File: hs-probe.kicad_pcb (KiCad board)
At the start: 4 copper layers, 36.5 x 14 mm, 52 parts, among them J1 USB_C_Receptacle_USB2.0, J2 Castellated Vias, J3 Castellated Vias, J4 Castellated Vias, U1 STM32F723IEKx, U2 DSC6003HI2A-012.0000T, U3 MIC5259, U4 NUF8401MNT4G, U5 STDC14, U6 SOICbite_SWD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

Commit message: Minor PCB cleanup, more GND vias
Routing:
- net +3V3: track 79.5 -> 85.0 mm
- net /D_FS_N: track 18.4 -> 20.2 mm
- net /T_SWDCLK_JCLK: track 12.3 -> 10.9 mm
- net GND: vias 68 -> 73

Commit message: Updated design from review comment
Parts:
- added R9: 1k, passive:R_0402, F.Cu at (174.3, 86.0)
- J4: footprint connectors:1x4_1.5mm_castellated -> connectors:1x3_1.5mm_castellated
- U3, U7: value MIC5259 -> MIC5353; footprint dfn:DFN-6-1EP_2x2mm_P0.65mm_EP1x1.6mm -> dfn:DFN-6-1EP_1.6x1.6mm_P0.5mm_EP0.5x1.26mm
- moved J4 1.50 mm to (179.0, 79.0)
- moved C25 1.20 mm to (174.3, 86.8)
- moved U3 0.60 mm to (174.8, 88.4)
- moved C2 0.10 mm to (173.0, 83.1), turned to 270 degrees
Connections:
- C27 pad 1: /T_VCC_PWR -> /T_VCC
- J4 pad 3: /T_VCC_PWR -> /T_VCC
- U1 pad E15: Net-(U1-PadE15) -> /FS_VBUS
- U1 pad P13: Net-(U1-PadP13) -> /FS_VBUS
- U5 pad 2: /T_VCC_PWR -> /T_VCC
- U7 pad 4: /T_VCC_PWR -> /T_VCC
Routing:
- net /T_VCC_PWR: track 42.4 -> 0.00 mm, vias 3 -> 0
- net /T_VCC: track 49.8 -> 82.1 mm, vias 2 -> 7
- net /FS_VBUS: track 0.00 -> 16.1 mm, vias 0 -> 3
- net GND: track 77.8 -> 91.4 mm, vias 73 -> 76
- net +3V3: track 85.0 -> 77.2 mm
- net /USB_SEL: track 11.8 -> 18.7 mm
- net +5V: track 65.8 -> 70.3 mm, vias 5 -> 7
- net Net-(J1-PadA5): track 16.0 -> 19.0 mm
- net /D_FS_N: track 20.2 -> 18.3 mm
- net Net-(C24-Pad1): track 31.3 -> 29.6 mm
- net /SPI2_MOSI: track 12.2 -> 13.7 mm
- net /GPIO2: track 8.49 -> 9.99 mm
- net /GPIO1: track 9.45 -> 11.0 mm
- net /T_VCC_MEAS: track 20.8 -> 20.0 mm
- net /RPHY: track 2.14 -> 2.87 mm
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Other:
- net class Default: clearance 0.124 -> 0.1
- rule trace_clearance: 0.124 -> 0.1
- board text added: "VDet/3V"
- board text removed: "3V"
- board text removed: "VDet"

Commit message: Major schematic cleanup
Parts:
- U1: value STM32F723IEKx -> hs-probe-stm32
- U2: value DSC6003HI2A-012.0000T -> 12 MHz
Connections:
- U1 pad D13: Net-(U1-PadD13) -> (no net)
- U1 pad E12: Net-(U1-PadE12) -> (no net)
- U1 pad E13: Net-(U1-PadE13) -> (no net)
- U1 pad E2: Net-(U1-PadE2) -> (no net)
- U1 pad F4: Net-(U1-PadF4) -> (no net)
- U1 pad G4: Net-(U1-PadG4) -> (no net)
- U1 pad H2: Net-(U1-PadH2) -> (no net)
- U1 pad H3: Net-(U1-PadH3) -> (no net)
- U1 pad H4: Net-(U1-PadH4) -> (no net)
- U1 pad J2: Net-(U1-PadJ2) -> (no net)
- U1 pad J3: Net-(U1-PadJ3) -> (no net)
- U1 pad J4: Net-(U1-PadJ4) -> (no net)
- U1 pad K1: Net-(U1-PadK1) -> (no net)
- U1 pad K12: Net-(U1-PadK12) -> (no net)
- U1 pad K2: Net-(U1-PadK2) -> (no net)
- U1 pad K3: Net-(U1-PadK3) -> (no net)
- U1 pad L1: Net-(U1-PadL1) -> (no net)
- U1 pad L12: Net-(U1-PadL12) -> (no net)
- U1 pad L13: Net-(U1-PadL13) -> (no net)
- U1 pad L2: Net-(U1-PadL2) -> (no net)
- U1 pad L3: Net-(U1-PadL3) -> (no net)
- U1 pad M11: Net-(U1-PadM11) -> (no net)
- U1 pad M12: Net-(U1-PadM12) -> (no net)
- U1 pad M13: Net-(U1-PadM13) -> (no net)
- U1 pad N12: Net-(U1-PadN12) -> (no net)
- U1 pad N6: Net-(U1-PadN6) -> (no net)
- U1 pad P6: Net-(U1-PadP6) -> (no net)
- U1 pad P7: Net-(U1-PadP7) -> (no net)
- U1 pad R6: Net-(U1-PadR6) -> (no net)
- U1 pad R7: Net-(U1-PadR7) -> (no net)

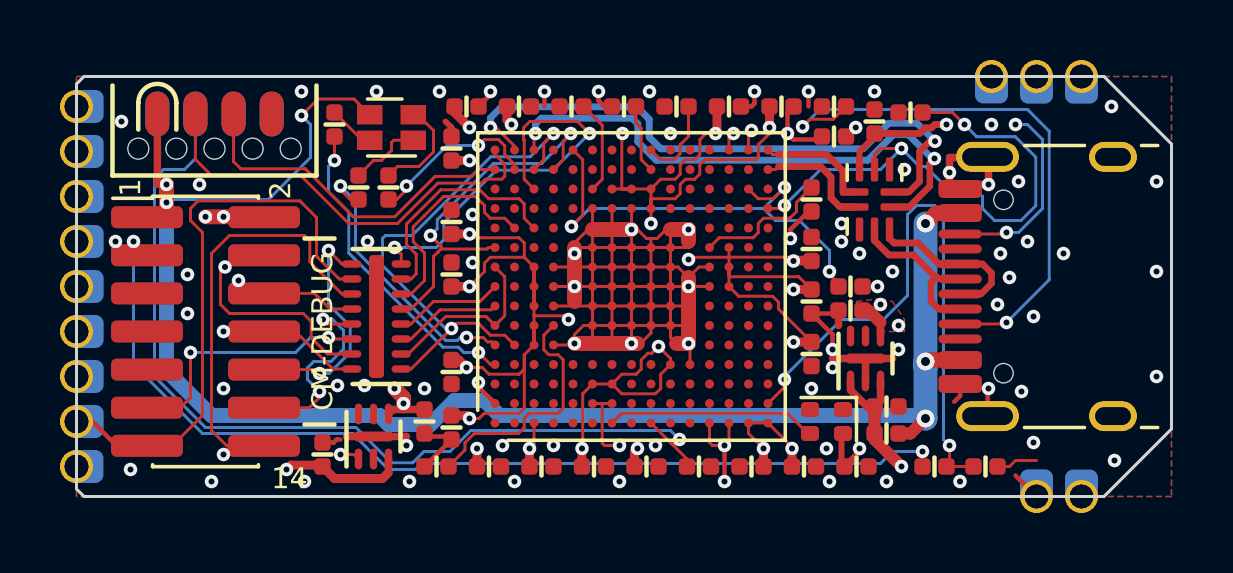
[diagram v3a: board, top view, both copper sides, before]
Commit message: Moved to tag connect
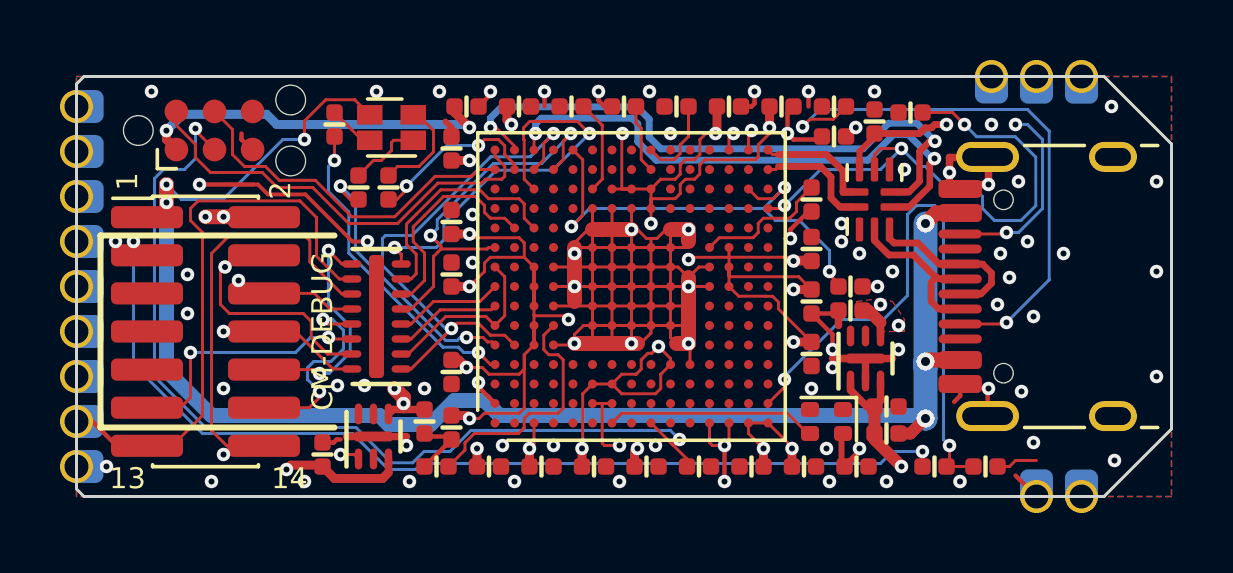
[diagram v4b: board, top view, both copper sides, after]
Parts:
- removed U6: SOICbite_SWD, connectors:SOICbiteSmall
- added J5: tag-connect-swd, Connector:Tag-Connect_TC2030-IDC-NL_2x03_P1.27mm_Vertical, F.Cu at (153.1, 80.8)
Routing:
- net +3V3: track 77.2 -> 88.4 mm, vias 27 -> 28
- net GND: track 91.4 -> 97.6 mm, vias 76 -> 75
- net +5V: track 70.3 -> 66.5 mm
- net /NRST: track 31.4 -> 31.8 mm, vias 1 -> 2
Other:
- board text added: "13"

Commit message: Added license, dimensions and manufacturing specs
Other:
- board text added: "90 Ohm diff."
- board text added: "LICENSE: This work is licensed under CERN-OHL-P."
- board text added: "Stackup: 4 Layer, 1.6mm L1 (TOP) = signals L2 = GND L3 = Power L4 (BOT) = signals Impedance: 90 Ohm differential, L1->L2 Tolerances: Min trace: 0.1mm Min via drill: 0.2mm Min via annular: 0.15mm Min clearance: 0.1mm Min component: 0402 Material: FR4 Copper: Top: 35um Bot: 35um Surface Finish: Top: ENIG Bot: ENIG Silkscreen: Top: White Bot: White Soldermask: Top: Green Bot: Green Special features: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"

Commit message: Updated 3D models to FTSH-107-01-L-DV-K
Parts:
- U5: footprint connectors:PinHeader_2x07_P1.27mm_Vertical_SMD -> connectors:PinHeader_2x07_FTSH-107-01-L-DV-K

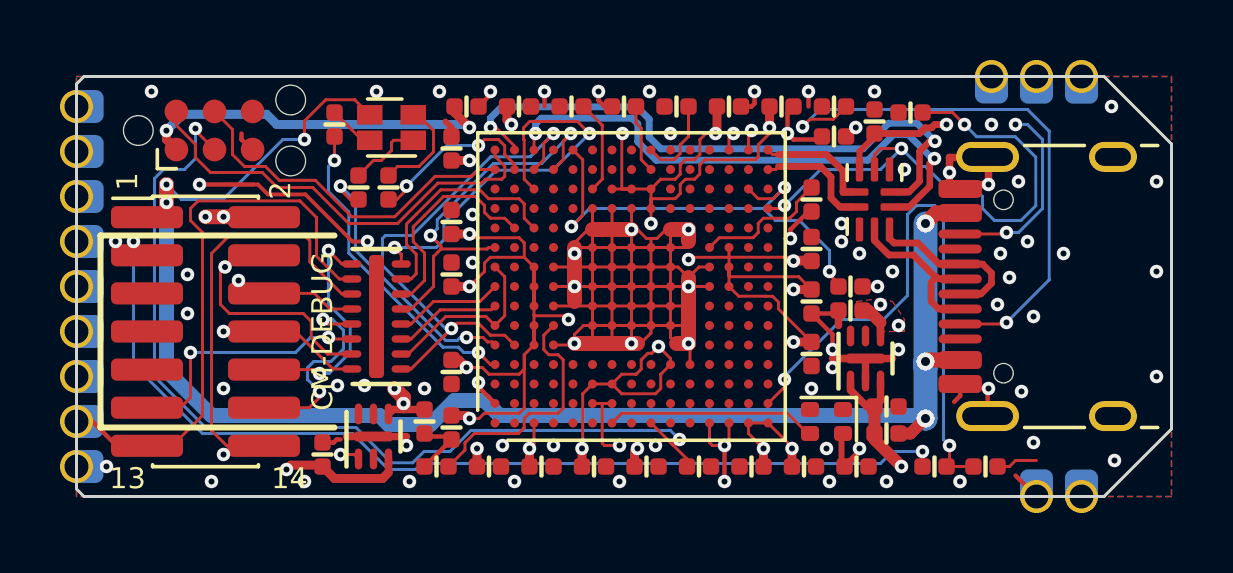
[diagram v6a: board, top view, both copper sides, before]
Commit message: Thickened up power traces under MCU
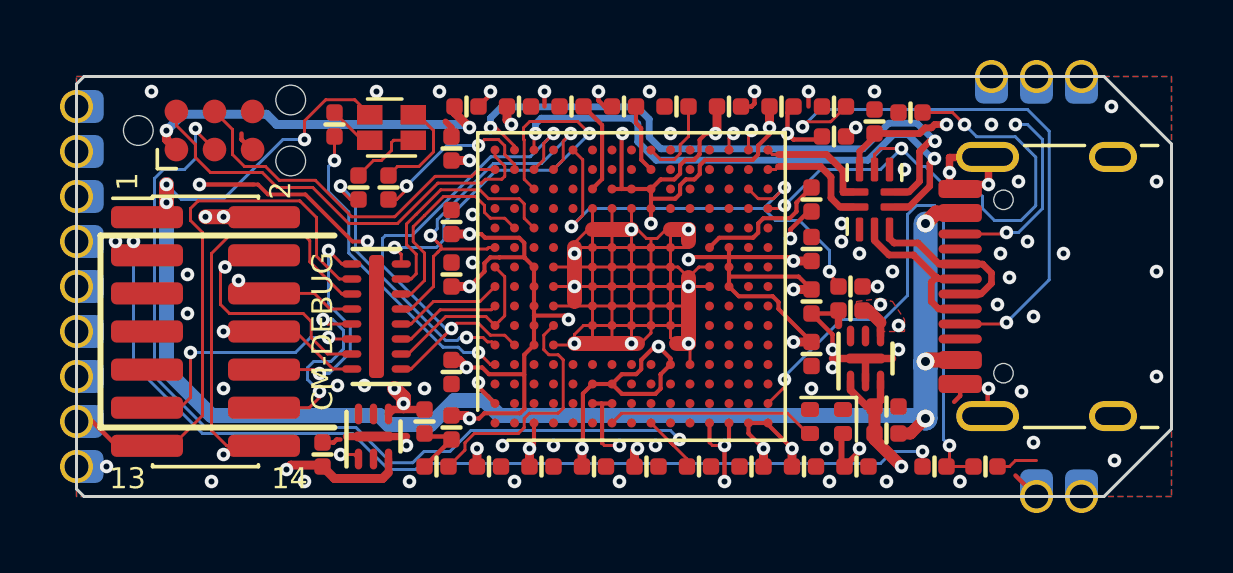
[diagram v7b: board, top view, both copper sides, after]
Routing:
- net GND: track 97.6 -> 98.3 mm

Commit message: Now using a 2x1.6mm crystal
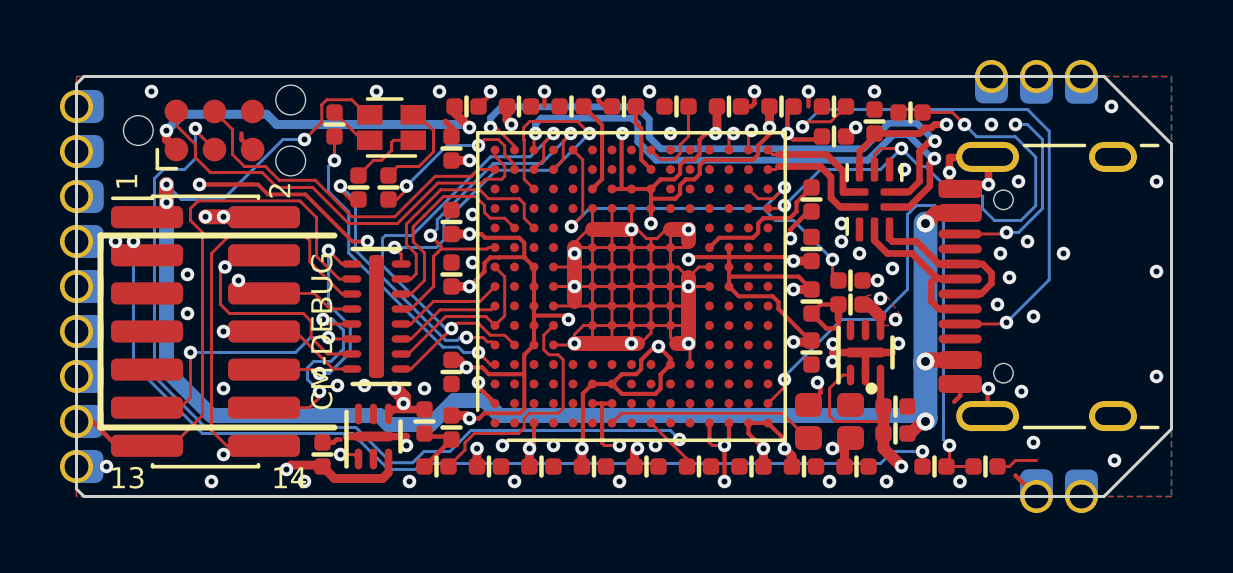
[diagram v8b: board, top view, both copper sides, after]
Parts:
- U2: footprint crystals:Oscillator_SMD_Abracon_ASCO-4Pin_1.6x1.2mm -> crystals:Crystal_4Pin_2.0x1.6mm
- moved C26 0.30 mm to (175.8, 90.0)
- moved FB1 0.30 mm to (175.8, 90.9)
- moved C25 0.20 mm to (174.3, 86.6)
- moved R9 0.20 mm to (174.3, 85.8)
- moved U3 0.20 mm to (174.8, 88.2)
- moved U2 0.10 mm to (173.6, 90.5), turned to 180 degrees
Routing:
- net Net-(C24-Pad1): track 29.6 -> 31.7 mm
- net GND: track 98.3 -> 100.3 mm, vias 75 -> 74
